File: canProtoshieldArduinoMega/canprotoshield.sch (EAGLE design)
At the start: 55 parts, among them CN1 1X4-3.5MM, CN10 1X4-3.5MM, CN11 1X4-3.5MM, CN12 1X4-3.5MM, CN13 1X4-3.5MM, CN14 1X4-3.5MM, CN15 1X4-3.5MM, CN16 1X4-3.5MM, CN17 1X4-3.5MM, CN18 1X4-3.5MM, CN19 1X4-3.5MM, CN2 1X4-3.5MM, CN20 1X4-3.5MM, CN21 1X4-3.5MM, CN22 1X4-3.5MM, CN23 1X4-3.5MM, CN24 1X4-3.5MM, CN25 1X4-3.5MM, CN26 1X4-3.5MM, CN27 1X4-3.5MM, CN28 1X4-3.5MM, CN29 1X4-3.5MM, CN3 1X4-3.5MM, CN30 1X4-3.5MM, CN31 1X4-3.5MM, CN32 1X4-3.5MM, CN33 1X4-3.5MM, CN34 1X4-3.5MM, CN4 1X4-3.5MM, CN5 1X4-3.5MM, CN6 1X4-3.5MM, CN7 1X4-3.5MM, CN8 1X4-3.5MM, CN9 1X4-3.5MM, U2 MCP2551, U3 ARDUINO-MEGAFULL

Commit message: Wiring.
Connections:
- removed net N$31: BUS_GND.1
- net GND: now also BUS_GND.1
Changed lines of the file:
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@@
 </instances>
 <busses>
-<bus name="B$1">
+<bus name="GND">
 <segment>
 <wire x1="274.32" y1="-45.72" x2="274.32" y2="-99.06" width="0.762" layer="92"/>
 </segment>
 </bus>
-<bus name="B$2">
+<bus name="VCC">
 <segment>
 <wire x1="256.54" y1="-45.72" x2="256.54" y2="-99.06" width="0.762" layer="92"/>
@@
 </segment>
 <segment>
-<wire x1="274.32" y1="-45.72" x2="269.24" y2="-45.72" width="0.1524" layer="91"/>
-</segment>
-<segment>
 <pinref part="U3" gate="G$1" pin="GND@0"/>
 <junction x="144.78" y="-15.24"/>
@@
 <junction x="144.78" y="-22.86"/>
 <wire x1="144.78" y1="-22.86" x2="137.16" y2="-22.86" width="0.1524" layer="91"/>
+</segment>
+<segment>
+<pinref part="BUS_GND" gate="A" pin="1"/>
+<junction x="274.32" y="-45.72"/>
+<wire x1="274.32" y1="-45.72" x2="269.24" y2="-45.72" width="0.1524" layer="91"/>
+<label x="269.24" y="-45.72" size="1.778" layer="95"/>
 </segment>
 </net>
@@
 <segment>
 <wire x1="256.54" y1="-45.72" x2="248.92" y2="-45.72" width="0.1524" layer="91"/>
+<label x="248.92" y="-45.72" size="1.778" layer="95"/>
 </segment>
 </net>
@@
 </segment>
 </net>
-<net name="N$31" class="0">
-<segment>
-<pinref part="BUS_GND" gate="A" pin="1"/>
-<junction x="274.32" y="-45.72"/>
-</segment>
-</net>

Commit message: Last edit need revision
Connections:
- net 10: now also CN20.3; no longer CN20.4
- net 11: now also CN20.2; no longer CN20.3
- net 12: now also CN20.1; no longer CN20.2
- net 13: no longer CN20.1
- net 2: now also CN22.3; no longer R3.2, S_CBUS.3, S_CBUS.4
- net 21: now also R3.2, S_CBUS.3, S_CBUS.4
- net 3: now also CN22.2; no longer CN22.3
- net 4: now also CN22.1; no longer CN22.2
- net 5: now also CN21.4; no longer CN22.1
- net 6: now also CN21.3; no longer CN21.4
- net 7: now also CN21.2; no longer CN21.3
- net 8: now also CN21.1; no longer CN21.2
- net 9: now also CN20.4; no longer CN21.1
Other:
- moved on the sheet: R3, S_CBUS
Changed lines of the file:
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@@
 <instance part="R2" gate="G$1" x="25.4" y="71.12"/>
 <instance part="RESET" gate="S" x="114.3" y="63.5"/>
-<instance part="S_CBUS" gate="S" x="119.38" y="17.78"/>
+<instance part="S_CBUS" gate="S" x="81.28" y="25.4"/>
 <instance part="U$1" gate="G$1" x="25.4" y="7.62"/>
 <instance part="C3" gate="G$1" x="-5.08" y="15.24" rot="R90"/>
@@
 <instance part="GND" gate="G$1" x="71.12" y="43.18"/>
 <instance part="VCC" gate="G$1" x="60.96" y="48.26"/>
-<instance part="R3" gate="G$1" x="127" y="10.16"/>
+<instance part="R3" gate="G$1" x="88.9" y="17.78"/>
 <instance part="U3" gate="G$1" x="165.1" y="25.4"/>
 <instance part="CN1" gate="G$1" x="-27.94" y="53.34" rot="R180"/>
@@
 <segment>
 <pinref part="S_CBUS" gate="S" pin="1"/>
-<wire x1="114.3" y1="17.78" x2="111.76" y2="17.78" width="0.1524" layer="91"/>
-<junction x="111.76" y="17.78"/>
-<wire x1="111.76" y1="17.78" x2="109.22" y2="17.78" width="0.1524" layer="91"/>
-<wire x1="111.76" y1="17.78" x2="111.76" y2="15.24" width="0.1524" layer="91"/>
+<wire x1="76.2" y1="25.4" x2="73.66" y2="25.4" width="0.1524" layer="91"/>
+<junction x="73.66" y="25.4"/>
+<wire x1="73.66" y1="25.4" x2="71.12" y2="25.4" width="0.1524" layer="91"/>
+<wire x1="73.66" y1="25.4" x2="73.66" y2="22.86" width="0.1524" layer="91"/>
 <pinref part="S_CBUS" gate="S" pin="2"/>
-<wire x1="111.76" y1="15.24" x2="114.3" y2="15.24" width="0.1524" layer="91"/>
-<label x="109.22" y="17.78" size="1.778" layer="95"/>
+<wire x1="73.66" y1="22.86" x2="76.2" y2="22.86" width="0.1524" layer="91"/>
+<label x="71.12" y="25.4" size="1.778" layer="95"/>
 </segment>
 <segment>
@@
 <segment>
 <pinref part="R3" gate="G$1" pin="1"/>
-<wire x1="121.92" y1="10.16" x2="114.3" y2="10.16" width="0.1524" layer="91"/>
-<label x="114.3" y="10.16" size="1.778" layer="95"/>
+<wire x1="83.82" y1="17.78" x2="76.2" y2="17.78" width="0.1524" layer="91"/>
+<label x="76.2" y="17.78" size="1.778" layer="95"/>
 </segment>
 <segment>
@@
 </segment>
 </net>
-<net name="2" class="0">
-<segment>
-<pinref part="S_CBUS" gate="S" pin="4"/>
-<wire x1="124.46" y1="15.24" x2="129.54" y2="15.24" width="0.1524" layer="91"/>
-<junction x="129.54" y="15.24"/>
-<pinref part="S_CBUS" gate="S" pin="3"/>
-<wire x1="124.46" y1="17.78" x2="129.54" y2="17.78" width="0.1524" layer="91"/>
-<wire x1="129.54" y1="15.24" x2="129.54" y2="17.78" width="0.1524" layer="91"/>
-<wire x1="129.54" y1="15.24" x2="132.08" y2="15.24" width="0.1524" layer="91"/>
-<pinref part="R3" gate="G$1" pin="2"/>
-<wire x1="132.08" y1="15.24" x2="132.08" y2="12.7" width="0.1524" layer="91"/>
-<junction x="132.08" y="12.7"/>
-<wire x1="132.08" y1="12.7" x2="132.08" y2="10.16" width="0.1524" layer="91"/>
-<pinref part="U3" gate="G$1" pin="2"/>
-<wire x1="132.08" y1="12.7" x2="144.78" y2="12.7" width="0.1524" layer="91"/>
-</segment>
-</net>
 <net name="VIN" class="0">
 <segment>
@@
 </segment>
 <segment>
-<pinref part="CN22" gate="G$1" pin="3"/>
-<junction x="22.86" y="-121.92"/>
-<label x="22.86" y="-121.92" size="1.778" layer="95"/>
-</segment>
-</net>
-<net name="4" class="0">
-<segment>
-<pinref part="U3" gate="G$1" pin="4"/>
-<wire x1="144.78" y1="7.62" x2="139.7" y2="7.62" width="0.1524" layer="91"/>
-</segment>
-<segment>
 <pinref part="CN22" gate="G$1" pin="2"/>
 <junction x="22.86" y="-124.46"/>
@@
 </segment>
 </net>
-<net name="5" class="0">
-<segment>
-<pinref part="U3" gate="G$1" pin="5"/>
-<wire x1="144.78" y1="5.08" x2="139.7" y2="5.08" width="0.1524" layer="91"/>
+<net name="4" class="0">
+<segment>
+<pinref part="U3" gate="G$1" pin="4"/>
+<wire x1="144.78" y1="7.62" x2="139.7" y2="7.62" width="0.1524" layer="91"/>
 </segment>
 <segment>
@@
 </segment>
 </net>
-<net name="6" class="0">
-<segment>
-<pinref part="U3" gate="G$1" pin="6"/>
-<wire x1="144.78" y1="2.54" x2="139.7" y2="2.54" width="0.1524" layer="91"/>
+<net name="5" class="0">
+<segment>
+<pinref part="U3" gate="G$1" pin="5"/>
+<wire x1="144.78" y1="5.08" x2="139.7" y2="5.08" width="0.1524" layer="91"/>
 </segment>
 <segment>
@@
 </segment>
 </net>
-<net name="7" class="0">
-<segment>
-<pinref part="U3" gate="G$1" pin="7"/>
-<wire x1="144.78" y1="0" x2="139.7" y2="0" width="0.1524" layer="91"/>
+<net name="6" class="0">
+<segment>
+<pinref part="U3" gate="G$1" pin="6"/>
+<wire x1="144.78" y1="2.54" x2="139.7" y2="2.54" width="0.1524" layer="91"/>
 </segment>
 <segment>
@@
 </segment>
 </net>
-<net name="8" class="0">
-<segment>
-<pinref part="U3" gate="G$1" pin="8"/>
-<wire x1="144.78" y1="-2.54" x2="139.7" y2="-2.54" width="0.1524" layer="91"/>
+<net name="7" class="0">
+<segment>
+<pinref part="U3" gate="G$1" pin="7"/>
+<wire x1="144.78" y1="0" x2="139.7" y2="0" width="0.1524" layer="91"/>
 </segment>
 <segment>
@@
 </segment>
 </net>
-<net name="9" class="0">
-<segment>
-<pinref part="U3" gate="G$1" pin="9"/>
-<wire x1="144.78" y1="-5.08" x2="139.7" y2="-5.08" width="0.1524" layer="91"/>
+<net name="8" class="0">
+<segment>
+<pinref part="U3" gate="G$1" pin="8"/>
+<wire x1="144.78" y1="-2.54" x2="139.7" y2="-2.54" width="0.1524" layer="91"/>
 </segment>
 <segment>
@@
 </segment>
 </net>
-<net name="10" class="0">
-<segment>
-<pinref part="U3" gate="G$1" pin="10"/>
-<wire x1="144.78" y1="-7.62" x2="139.7" y2="-7.62" width="0.1524" layer="91"/>
+<net name="9" class="0">
+<segment>
+<pinref part="U3" gate="G$1" pin="9"/>
+<wire x1="144.78" y1="-5.08" x2="139.7" y2="-5.08" width="0.1524" layer="91"/>
 </segment>
 <segment>
@@
 </segment>
 </net>
-<net name="11" class="0">
-<segment>
-<pinref part="U3" gate="G$1" pin="11"/>
-<wire x1="144.78" y1="-10.16" x2="139.7" y2="-10.16" width="0.1524" layer="91"/>
+<net name="10" class="0">
+<segment>
+<pinref part="U3" gate="G$1" pin="10"/>
+<wire x1="144.78" y1="-7.62" x2="139.7" y2="-7.62" width="0.1524" layer="91"/>
 </segment>
 <segment>
@@
 </segment>
 </net>
-<net name="12" class="0">
-<segment>
-<pinref part="U3" gate="G$1" pin="12"/>
-<wire x1="144.78" y1="-12.7" x2="139.7" y2="-12.7" width="0.1524" layer="91"/>
+<net name="11" class="0">
+<segment>
+<pinref part="U3" gate="G$1" pin="11"/>
+<wire x1="144.78" y1="-10.16" x2="139.7" y2="-10.16" width="0.1524" layer="91"/>
 </segment>
 <segment>
@@
 </segment>
 </net>
+<net name="12" class="0">
+<segment>
+<pinref part="U3" gate="G$1" pin="12"/>
+<wire x1="144.78" y1="-12.7" x2="139.7" y2="-12.7" width="0.1524" layer="91"/>
+</segment>
+<segment>
+<pinref part="CN20" gate="G$1" pin="1"/>
+<junction x="58.42" y="-106.68"/>
+<label x="58.42" y="-106.68" size="1.778" layer="95"/>
+</segment>
+</net>
 <net name="14" class="0">
 <segment>
@@
 <pinref part="U3" gate="G$1" pin="21(SCL)"/>
 <wire x1="185.42" y1="55.88" x2="193.04" y2="55.88" width="0.1524" layer="91"/>
+</segment>
+<segment>
+<pinref part="S_CBUS" gate="S" pin="3"/>
+<pinref part="S_CBUS" gate="S" pin="4"/>
+<wire x1="86.36" y1="25.4" x2="86.36" y2="22.86" width="0.1524" layer="91"/>
+<junction x="86.36" y="22.86"/>
+<pinref part="R3" gate="G$1" pin="2"/>
+<junction x="93.98" y="17.78"/>
+<wire x1="86.36" y1="22.86" x2="93.98" y2="22.86" width="0.1524" layer="91"/>
+<wire x1="93.98" y1="22.86" x2="93.98" y2="17.78" width="0.1524" layer="91"/>
+<wire x1="93.98" y1="17.78" x2="99.06" y2="17.78" width="0.1524" layer="91"/>
+<label x="99.06" y="17.78" size="1.778" layer="95"/>
 </segment>
 </net>
@@
 <wire x1="185.42" y1="76.2" x2="193.04" y2="76.2" width="0.1524" layer="91"/>
 </segment>
-<segment>
-<pinref part="CN20" gate="G$1" pin="1"/>
-<junction x="58.42" y="-106.68"/>
-<label x="58.42" y="-106.68" size="1.778" layer="95"/>
-</segment>
 </net>
 <net name="N$14" class="0">
@@
 </segment>
 </net>
+<net name="2" class="0">
+<segment>
+<pinref part="CN22" gate="G$1" pin="3"/>
+<junction x="22.86" y="-121.92"/>
+</segment>
+<segment>
+<pinref part="U3" gate="G$1" pin="2"/>
+<wire x1="144.78" y1="12.7" x2="139.7" y2="12.7" width="0.1524" layer="91"/>
+</segment>
+</net>

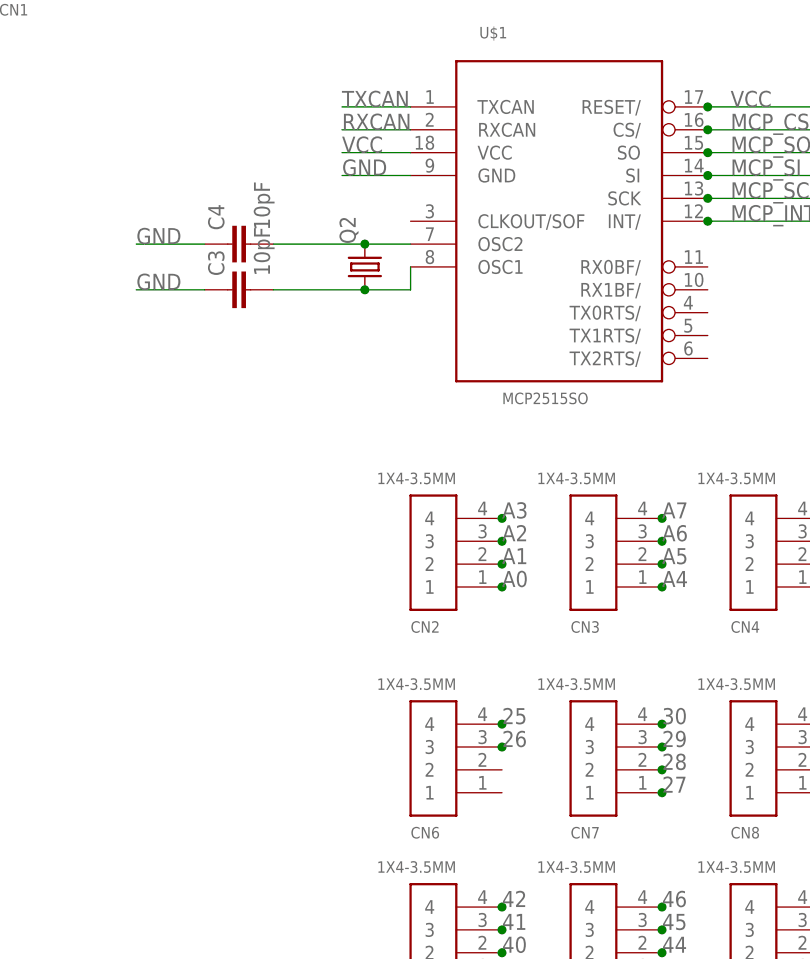
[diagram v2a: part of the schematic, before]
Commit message: Crystal change
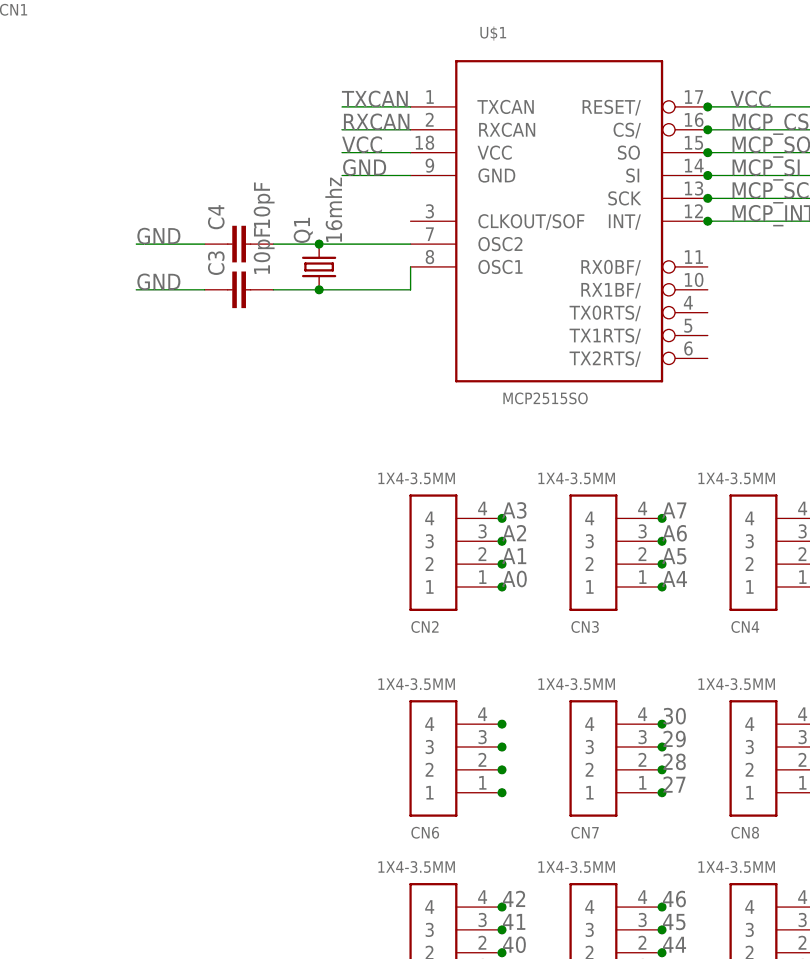
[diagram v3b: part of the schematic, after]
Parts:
- removed Q2: (no value), adafruit:CRYSTALCTS406
- added Q1: 16mhz, adafruit:CRYSTALHC49S
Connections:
- new net N$53: CN6.4
- net 24: now also CN6.3
- net 25: now also CN6.2; no longer CN6.4
- net 26: now also CN6.1; no longer CN6.3
- net N$1: now also Q1.2; no longer Q2.2
- net N$2: now also Q1.1; no longer Q2.1
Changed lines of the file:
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@@
 <part name="CN33" library="Arduino_merg" deviceset="1X4" device="-3.5MM"/>
 <part name="CN34" library="Arduino_merg" deviceset="1X4" device="-3.5MM"/>
-<part name="Q2" library="adafruit" deviceset="CRYSTAL" device="CTS406"/>
 <part name="JP1" library="adafruit" deviceset="PINHD-1X20" device="-BIG"/>
 <part name="JP2" library="adafruit" deviceset="PINHD-1X20" device="-BIG"/>
 <part name="JP3" library="pinhead" deviceset="PINHD-2X24" device=""/>
 <part name="JP4" library="pinhead" deviceset="PINHD-2X24" device=""/>
+<part name="Q1" library="adafruit" deviceset="CRYSTAL" device="HC49S" value="16mhz"/>
 </parts>
 <sheets>
@@
 <instance part="CN33" gate="G$1" x="116.84" y="-104.14" rot="R180"/>
 <instance part="CN34" gate="G$1" x="116.84" y="-127" rot="R180"/>
-<instance part="Q2" gate="G$1" x="7.62" y="17.78" rot="R90"/>
 <instance part="JP1" gate="A" x="187.96" y="-81.28"/>
 <instance part="JP2" gate="A" x="205.74" y="-81.28"/>
 <instance part="JP3" gate="A" x="322.58" y="-139.7"/>
 <instance part="JP4" gate="A" x="297.18" y="-139.7"/>
+<instance part="Q1" gate="G$1" x="2.54" y="17.78" rot="R90"/>
 </instances>
 <busses>
@@
 <pinref part="U$1" gate="G$1" pin="OSC2"/>
 <pinref part="C4" gate="G$1" pin="2"/>
-<wire x1="12.7" y1="20.32" x2="7.62" y2="20.32" width="0.1524" layer="91"/>
-<pinref part="Q2" gate="G$1" pin="2"/>
-<wire x1="7.62" y1="20.32" x2="-2.54" y2="20.32" width="0.1524" layer="91"/>
-<junction x="7.62" y="20.32"/>
+<wire x1="12.7" y1="20.32" x2="2.54" y2="20.32" width="0.1524" layer="91"/>
+<pinref part="Q1" gate="G$1" pin="2"/>
+<wire x1="2.54" y1="20.32" x2="-2.54" y2="20.32" width="0.1524" layer="91"/>
+<junction x="2.54" y="20.32"/>
 </segment>
 </net>
@@
 <wire x1="12.7" y1="17.78" x2="12.7" y2="15.24" width="0.1524" layer="91"/>
 <pinref part="C3" gate="G$1" pin="2"/>
-<wire x1="12.7" y1="15.24" x2="7.62" y2="15.24" width="0.1524" layer="91"/>
-<pinref part="Q2" gate="G$1" pin="1"/>
-<wire x1="7.62" y1="15.24" x2="-2.54" y2="15.24" width="0.1524" layer="91"/>
-<junction x="7.62" y="15.24"/>
+<wire x1="12.7" y1="15.24" x2="2.54" y2="15.24" width="0.1524" layer="91"/>
+<pinref part="Q1" gate="G$1" pin="1"/>
+<wire x1="2.54" y1="15.24" x2="-2.54" y2="15.24" width="0.1524" layer="91"/>
+<junction x="2.54" y="15.24"/>
 </segment>
 </net>
@@
 <wire x1="185.42" y1="48.26" x2="193.04" y2="48.26" width="0.1524" layer="91"/>
 </segment>
+<segment>
+<pinref part="CN6" gate="G$1" pin="3"/>
+<junction x="22.86" y="-35.56"/>
+</segment>
 </net>
 <net name="25" class="0">
@@
 </segment>
 <segment>
-<pinref part="CN6" gate="G$1" pin="4"/>
-<junction x="22.86" y="-33.02"/>
-<label x="22.86" y="-33.02" size="1.778" layer="95"/>
+<pinref part="CN6" gate="G$1" pin="2"/>
+<junction x="22.86" y="-38.1"/>
 </segment>
 </net>
@@
 </segment>
 <segment>
-<pinref part="CN6" gate="G$1" pin="3"/>
-<junction x="22.86" y="-35.56"/>
-<label x="22.86" y="-35.56" size="1.778" layer="95"/>
+<pinref part="CN6" gate="G$1" pin="1"/>
+<junction x="22.86" y="-40.64"/>
 </segment>
 </net>
@@
 </segment>
 </net>
+<net name="N$53" class="0">
+<segment>
+<pinref part="CN6" gate="G$1" pin="4"/>
+<junction x="22.86" y="-33.02"/>
+</segment>
+</net>
 </nets>
 </sheet>
 </sheets>
+<errors>
+</errors>
 </schematic>
 </drawing>
